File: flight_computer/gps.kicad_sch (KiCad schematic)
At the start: 12 parts, among them U6 YIC31612EBGG, U9 Antenna_GPS

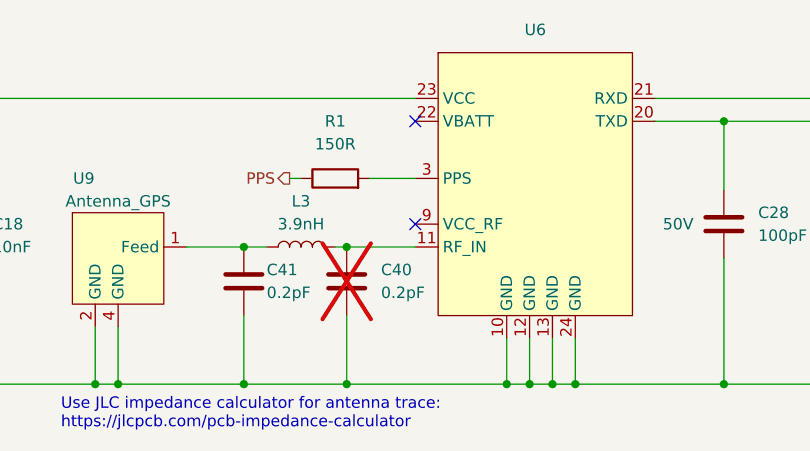
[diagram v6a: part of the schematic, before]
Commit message: Antenna routing, and other routing done
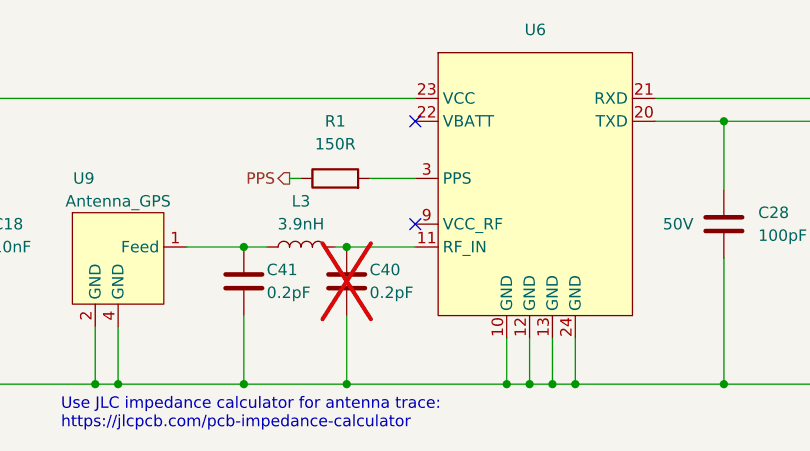
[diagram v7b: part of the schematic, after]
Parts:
- C40, C41: footprint Capacitor_SMD:C_0402_1005Metric -> Capacitor_SMD:C_0201_0603Metric; Manufacturer PN GJM1555C1HR20BB01D -> (none); Supplier Digikey -> (none); Supplier PN 490-3078-1-ND -> (none)
- L3: footprint Inductor_SMD:L_0402_1005Metric -> Inductor_SMD:L_0201_0603Metric; Manufacturer PN LRC0402CS3N9GV001T -> (none); Supplier Digikey -> (none); Supplier PN 712-LRC0402CS3N9GV001TCT-ND -> (none)
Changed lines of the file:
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@@
   (junction (at 85.09 119.38) (diameter 0) (color 0 0 0 0)
   )
+  (junction (at 128.27 104.14) (diameter 0) (color 0 0 0 0)
+  )
   (junction (at 85.09 87.63) (diameter 0) (color 0 0 0 0)
   )
@@
   )
   (junction (at 128.27 119.38) (diameter 0) (color 0 0 0 0)
-  )
-  (junction (at 128.27 104.14) (diameter 0) (color 0 0 0 0)
   )
   (junction (at 68.58 87.63) (diameter 0) (color 0 0 0 0)
@@
     (stroke (width 0) (type default))
   )
+  (wire (pts (xy 127 104.14) (xy 128.27 104.14))
+    (stroke (width 0) (type default))
+  )
+  (wire (pts (xy 151.13 119.38) (xy 153.67 119.38))
+    (stroke (width 0) (type default))
+  )
+  (wire (pts (xy 162.56 87.63) (xy 187.96 87.63))
+    (stroke (width 0) (type default))
+  )
+  (wire (pts (xy 212.09 90.17) (xy 219.71 90.17))
+    (stroke (width 0) (type default))
+  )
+  (wire (pts (xy 170.18 90.17) (xy 170.18 97.79))
+    (stroke (width 0) (type default))
+  )
   (wire (pts (xy 128.27 104.14) (xy 135.89 104.14))
-    (stroke (width 0) (type default))
-  )
-  (wire (pts (xy 127 104.14) (xy 128.27 104.14))
-    (stroke (width 0) (type default))
-  )
-  (wire (pts (xy 151.13 119.38) (xy 153.67 119.38))
-    (stroke (width 0) (type default))
-  )
-  (wire (pts (xy 162.56 87.63) (xy 187.96 87.63))
-    (stroke (width 0) (type default))
-  )
-  (wire (pts (xy 212.09 90.17) (xy 219.71 90.17))
-    (stroke (width 0) (type default))
-  )
-  (wire (pts (xy 170.18 90.17) (xy 170.18 97.79))
     (stroke (width 0) (type default))
   )
@@
       (effects (font (size 1.27 1.27)))
     )
-    (property "Footprint" "Inductor_SMD:L_0402_1005Metric" (at 123.19 104.14 0)
+    (property "Footprint" "Inductor_SMD:L_0201_0603Metric" (at 123.19 104.14 0)
       (effects (font (size 1.27 1.27)) hide)
     )
@@
       (effects (font (size 1.27 1.27)) hide)
     )
-    (property "Manufacturer PN" "LRC0402CS3N9GV001T" (at 123.19 104.14 0)
-      (effects (font (size 1.27 1.27)) hide)
-    )
-    (property "Supplier PN" "712-LRC0402CS3N9GV001TCT-ND" (at 123.19 104.14 0)
-      (effects (font (size 1.27 1.27)) hide)
-    )
-    (property "Supplier" "Digikey" (at 123.19 104.14 0)
+    (property "Manufacturer PN" "" (at 123.19 104.14 0)
+      (effects (font (size 1.27 1.27)) hide)
+    )
+    (property "Supplier PN" "" (at 123.19 104.14 0)
+      (effects (font (size 1.27 1.27)) hide)
+    )
+    (property "Supplier" "" (at 123.19 104.14 0)
       (effects (font (size 1.27 1.27)) hide)
     )
@@
     )
   )
-  (symbol (lib_id "Device:C") (at 128.27 107.95 0) (unit 1)
-    (in_bom yes) (on_board yes) (dnp yes) (fields_autoplaced)
-    (property "Reference" "C40" (at 132.08 106.68 0)
-      (effects (font (size 1.27 1.27)) (justify left))
-    )
-    (property "Value" "0.2pF" (at 132.08 109.22 0)
-      (effects (font (size 1.27 1.27)) (justify left))
-    )
-    (property "Footprint" "Capacitor_SMD:C_0402_1005Metric" (at 129.2352 111.76 0)
-      (effects (font (size 1.27 1.27)) hide)
-    )
-    (property "Datasheet" "https://search.murata.co.jp/Ceramy/image/img/A01X/G101/ENG/GJM1555C1HR20BB01-01.pdf" (at 128.27 107.95 0)
-      (effects (font (size 1.27 1.27)) hide)
-    )
-    (property "Manufacturer PN" "GJM1555C1HR20BB01D" (at 128.27 107.95 0)
-      (effects (font (size 1.27 1.27)) hide)
-    )
-    (property "Supplier PN" "490-3078-1-ND" (at 128.27 107.95 0)
-      (effects (font (size 1.27 1.27)) hide)
-    )
-    (property "Supplier" "Digikey" (at 128.27 107.95 0)
-      (effects (font (size 1.27 1.27)) hide)
-    )
-    (pin "1")
-    (pin "2")
-    (instances
-      (project "flight_computer"
-        (path "/89a81c02-14e9-456f-a334-ff69a24bd093/8a1e6a35-f87c-4284-aec3-66a93071d289"
-          (reference "C40") (unit 1)
-        )
-      )
-    )
-  )
   (symbol (lib_id "Device:C") (at 116.84 107.95 0) (unit 1)
     (in_bom yes) (on_board yes) (dnp no)
@@
       (effects (font (size 1.27 1.27)) (justify left))
     )
-    (property "Footprint" "Capacitor_SMD:C_0402_1005Metric" (at 117.8052 111.76 0)
-      (effects (font (size 1.27 1.27)) hide)
-    )
-    (property "Datasheet" "https://search.murata.co.jp/Ceramy/image/img/A01X/G101/ENG/GJM1555C1HR20BB01-01.pdf" (at 116.84 107.95 0)
-      (effects (font (size 1.27 1.27)) hide)
-    )
-    (property "Manufacturer PN" "GJM1555C1HR20BB01D" (at 116.84 107.95 0)
-      (effects (font (size 1.27 1.27)) hide)
-    )
-    (property "Supplier PN" "490-3078-1-ND" (at 116.84 107.95 0)
-      (effects (font (size 1.27 1.27)) hide)
-    )
-    (property "Supplier" "Digikey" (at 116.84 107.95 0)
+    (property "Footprint" "Capacitor_SMD:C_0201_0603Metric" (at 117.8052 111.76 0)
+      (effects (font (size 1.27 1.27)) hide)
+    )
+    (property "Datasheet" "" (at 116.84 107.95 0)
+      (effects (font (size 1.27 1.27)) hide)
+    )
+    (property "Manufacturer PN" "" (at 116.84 107.95 0)
+      (effects (font (size 1.27 1.27)) hide)
+    )
+    (property "Supplier PN" "" (at 116.84 107.95 0)
+      (effects (font (size 1.27 1.27)) hide)
+    )
+    (property "Supplier" "" (at 116.84 107.95 0)
       (effects (font (size 1.27 1.27)) hide)
     )
@@
         )
       )
+    )
+  )
+  (symbol (lib_id "Device:C") (at 128.27 107.95 0) (unit 1)
+    (in_bom yes) (on_board yes) (dnp yes)
+    (property "Reference" "C40" (at 130.81 106.68 0)
+      (effects (font (size 1.27 1.27)) (justify left))
+    )
+    (property "Value" "0.2pF" (at 130.81 109.22 0)
+      (effects (font (size 1.27 1.27)) (justify left))
+    )
+    (property "Footprint" "Capacitor_SMD:C_0201_0603Metric" (at 129.2352 111.76 0)
+      (effects (font (size 1.27 1.27)) hide)
+    )
+    (property "Datasheet" "" (at 128.27 107.95 0)
+      (effects (font (size 1.27 1.27)) hide)
+    )
+    (property "Manufacturer PN" "" (at 128.27 107.95 0)
+      (effects (font (size 1.27 1.27)) hide)
+    )
+    (property "Supplier PN" "" (at 128.27 107.95 0)
+      (effects (font (size 1.27 1.27)) hide)
+    )
+    (property "Supplier" "" (at 128.27 107.95 0)
+      (effects (font (size 1.27 1.27)) hide)
+    )
+    (pin "1")
+    (pin "2")
+    (instances
+      (project "flight_computer"
+        (path "/89a81c02-14e9-456f-a334-ff69a24bd093/8a1e6a35-f87c-4284-aec3-66a93071d289"
+          (reference "C40") (unit 1)
+        )
+      )

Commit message: Moving antenna and removing matching circuit
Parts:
- removed C40, C41: 0.2pF, Capacitor_SMD:C_0201_0603Metric, symbol Device:C
- removed L3: 3.9nH, Inductor_SMD:L_0201_0603Metric, symbol Device:L
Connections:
- net at U9.1 (Feed): now also U6.11 (RF_IN)
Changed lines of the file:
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@@
   (junction (at 85.09 119.38) (diameter 0) (color 0 0 0 0)
   )
-  (junction (at 128.27 104.14) (diameter 0) (color 0 0 0 0)
-  )
   (junction (at 85.09 87.63) (diameter 0) (color 0 0 0 0)
   )
@@
   (junction (at 148.59 119.38) (diameter 0) (color 0 0 0 0)
   )
-  (junction (at 116.84 119.38) (diameter 0) (color 0 0 0 0)
-  )
   (junction (at 151.13 119.38) (diameter 0) (color 0 0 0 0)
   )
@@
   (junction (at 170.18 119.38) (diameter 0) (color 0 0 0 0)
   )
-  (junction (at 128.27 119.38) (diameter 0) (color 0 0 0 0)
-  )
   (junction (at 68.58 87.63) (diameter 0) (color 0 0 0 0)
-  )
-  (junction (at 116.84 104.14) (diameter 0) (color 0 0 0 0)
   )
   (junction (at 100.33 119.38) (diameter 0) (color 0 0 0 0)
@@
     (stroke (width 0) (type default))
   )
-  (wire (pts (xy 127 104.14) (xy 128.27 104.14))
-    (stroke (width 0) (type default))
-  )
   (wire (pts (xy 151.13 119.38) (xy 153.67 119.38))
     (stroke (width 0) (type default))
@@
     (stroke (width 0) (type default))
   )
-  (wire (pts (xy 128.27 104.14) (xy 135.89 104.14))
-    (stroke (width 0) (type default))
-  )
   (wire (pts (xy 187.96 119.38) (xy 187.96 105.41))
     (stroke (width 0) (type default))
@@
     (stroke (width 0) (type default))
   )
-  (wire (pts (xy 128.27 119.38) (xy 146.05 119.38))
+  (wire (pts (xy 102.87 119.38) (xy 146.05 119.38))
     (stroke (width 0) (type default))
   )
@@
     (stroke (width 0) (type default))
   )
-  (wire (pts (xy 102.87 119.38) (xy 116.84 119.38))
-    (stroke (width 0) (type default))
-  )
   (wire (pts (xy 62.23 119.38) (xy 68.58 119.38))
     (stroke (width 0) (type default))
@@
     (stroke (width 0) (type default))
   )
-  (wire (pts (xy 110.49 104.14) (xy 116.84 104.14))
+  (wire (pts (xy 110.49 104.14) (xy 135.89 104.14))
     (stroke (width 0) (type default))
   )
@@
     (stroke (width 0) (type default))
   )
-  (wire (pts (xy 116.84 119.38) (xy 128.27 119.38))
-    (stroke (width 0) (type default))
-  )
   (wire (pts (xy 68.58 106.68) (xy 68.58 119.38))
     (stroke (width 0) (type default))
   )
-  (wire (pts (xy 116.84 104.14) (xy 119.38 104.14))
-    (stroke (width 0) (type default))
-  )
   (wire (pts (xy 85.09 87.63) (xy 135.89 87.63))
     (stroke (width 0) (type default))
@@
     (stroke (width 0) (type default))
   )
-  (wire (pts (xy 116.84 111.76) (xy 116.84 119.38))
-    (stroke (width 0) (type default))
-  )
   (wire (pts (xy 68.58 99.06) (xy 68.58 87.63))
     (stroke (width 0) (type default))
@@
   )
   (wire (pts (xy 146.05 119.38) (xy 146.05 114.3))
-    (stroke (width 0) (type default))
-  )
-  (wire (pts (xy 128.27 111.76) (xy 128.27 119.38))
     (stroke (width 0) (type default))
   )
@@
   (hierarchical_label "RXD" (shape input) (at 219.71 87.63 0) (fields_autoplaced)
     (effects (font (size 1.27 1.27)) (justify left))
-  )
-  (symbol (lib_id "Device:L") (at 123.19 104.14 90) (unit 1)
-    (in_bom yes) (on_board yes) (dnp no) (fields_autoplaced)
-    (property "Reference" "L3" (at 123.19 99.06 90)
-      (effects (font (size 1.27 1.27)))
-    )
-    (property "Value" "3.9nH" (at 123.19 101.6 90)
-      (effects (font (size 1.27 1.27)))
-    )
-    (property "Footprint" "Inductor_SMD:L_0201_0603Metric" (at 123.19 104.14 0)
-      (effects (font (size 1.27 1.27)) hide)
-    )
-    (property "Datasheet" "https://www.johansontechnology.com/downloads/jti-cat-rf-ind.pdf" (at 123.19 104.14 0)
-      (effects (font (size 1.27 1.27)) hide)
-    )
-    (property "Manufacturer PN" "" (at 123.19 104.14 0)
-      (effects (font (size 1.27 1.27)) hide)
-    )
-    (property "Supplier PN" "" (at 123.19 104.14 0)
-      (effects (font (size 1.27 1.27)) hide)
-    )
-    (property "Supplier" "" (at 123.19 104.14 0)
-      (effects (font (size 1.27 1.27)) hide)
-    )
-    (pin "1")
-    (pin "2")
-    (instances
-      (project "flight_computer"
-        (path "/89a81c02-14e9-456f-a334-ff69a24bd093/8a1e6a35-f87c-4284-aec3-66a93071d289"
-          (reference "L3") (unit 1)
-        )
-      )
-    )
   )
   (symbol (lib_id "Device:C") (at 170.18 101.6 0) (unit 1)
@@
     )
   )
-  (symbol (lib_id "Device:C") (at 116.84 107.95 0) (unit 1)
-    (in_bom yes) (on_board yes) (dnp no)
-    (property "Reference" "C41" (at 119.38 106.68 0)
-      (effects (font (size 1.27 1.27)) (justify left))
-    )
-    (property "Value" "0.2pF" (at 119.38 109.22 0)
-      (effects (font (size 1.27 1.27)) (justify left))
-    )
-    (property "Footprint" "Capacitor_SMD:C_0201_0603Metric" (at 117.8052 111.76 0)
-      (effects (font (size 1.27 1.27)) hide)
-    )
-    (property "Datasheet" "" (at 116.84 107.95 0)
-      (effects (font (size 1.27 1.27)) hide)
-    )
-    (property "Manufacturer PN" "" (at 116.84 107.95 0)
-      (effects (font (size 1.27 1.27)) hide)
-    )
-    (property "Supplier PN" "" (at 116.84 107.95 0)
-      (effects (font (size 1.27 1.27)) hide)
-    )
-    (property "Supplier" "" (at 116.84 107.95 0)
-      (effects (font (size 1.27 1.27)) hide)
-    )
-    (pin "1")
-    (pin "2")
-    (instances
-      (project "flight_computer"
-        (path "/89a81c02-14e9-456f-a334-ff69a24bd093/8a1e6a35-f87c-4284-aec3-66a93071d289"
-          (reference "C41") (unit 1)
-        )
-      )
-    )
-  )
   (symbol (lib_id "Device:C") (at 68.58 102.87 0) (unit 1)
     (in_bom yes) (on_board yes) (dnp no)
@@
         )
       )
-    )
-  )
-  (symbol (lib_id "Device:C") (at 128.27 107.95 0) (unit 1)
-    (in_bom yes) (on_board yes) (dnp yes)
-    (property "Reference" "C40" (at 130.81 106.68 0)
-      (effects (font (size 1.27 1.27)) (justify left))
-    )
-    (property "Value" "0.2pF" (at 130.81 109.22 0)
-      (effects (font (size 1.27 1.27)) (justify left))
-    )
-    (property "Footprint" "Capacitor_SMD:C_0201_0603Metric" (at 129.2352 111.76 0)
-      (effects (font (size 1.27 1.27)) hide)
-    )
-    (property "Datasheet" "" (at 128.27 107.95 0)
-      (effects (font (size 1.27 1.27)) hide)
-    )
-    (property "Manufacturer PN" "" (at 128.27 107.95 0)
-      (effects (font (size 1.27 1.27)) hide)
-    )
-    (property "Supplier PN" "" (at 128.27 107.95 0)
-      (effects (font (size 1.27 1.27)) hide)
-    )
-    (property "Supplier" "" (at 128.27 107.95 0)
-      (effects (font (size 1.27 1.27)) hide)
-    )
-    (pin "1")
-    (pin "2")
-    (instances
-      (project "flight_computer"
-        (path "/89a81c02-14e9-456f-a334-ff69a24bd093/8a1e6a35-f87c-4284-aec3-66a93071d289"
-          (reference "C40") (unit 1)
-        )
-      )
